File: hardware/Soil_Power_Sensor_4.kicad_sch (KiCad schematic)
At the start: 15 parts, among them J3 UART, J5 Micro_SD_Card, SW1 BOOT, SW2 EN, U8 ESP32-C3-WROOM-02-N4

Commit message: Updated LCSC parts numbers
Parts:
- RN1: MPN (none) -> YC164-JR-1310KL
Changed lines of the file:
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@@
+			)
+		)
+		(property "MPN" " YC164-JR-1310KL"
+			(at 85.09 151.13 0)
+			(effects
+				(font
+					(size 1.27 1.27)
+				)
+				(hide yes)
 			)
 		)
@@
 			)
 		)
+		(property "MPN" " YC164-JR-1310KL"
+			(at 54.61 151.13 0)
+			(effects
+				(font
+					(size 1.27 1.27)
+				)
+				(hide yes)
+			)
+		)
 		(pin "2"
 		)
@@
 			)
 		)
+		(property "MPN" " YC164-JR-1310KL"
+			(at 74.93 151.13 0)
+			(effects
+				(font
+					(size 1.27 1.27)
+				)
+				(hide yes)
+			)
+		)
 		(pin "2"
 		)
@@
 			(at 64.77 151.13 0)
 			(effects
+				(font
+					(size 1.27 1.27)
+				)
+				(hide yes)
+			)
+		)
+		(property "MPN" " YC164-JR-1310KL"
+			(at 64.77 151.13 0)
+			(effects

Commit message: Updated BOM
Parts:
- SW1, SW2: LCSC C93157 -> C2837532
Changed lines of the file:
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@@
 			)
 		)
-		(property "LCSC" "C93157"
+		(property "LCSC" "C2837532"
 			(at 245.11 77.47 0)
 			(effects
@@
 			)
 		)
-		(property "LCSC" "C93157"
+		(property "LCSC" "C2837532"
 			(at 245.11 46.99 0)
 			(effects

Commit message: Regenerated files with kicad-cli script
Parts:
- RN1: LCSC (none) -> C110924
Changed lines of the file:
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@@
+			)
+		)
+		(property "LCSC" "C110924"
+			(at 85.09 151.13 0)
+			(effects
+				(font
+					(size 1.27 1.27)
+				)
+				(hide yes)
 			)
 		)
@@
 			)
 		)
+		(property "LCSC" "C110924"
+			(at 54.61 151.13 0)
+			(effects
+				(font
+					(size 1.27 1.27)
+				)
+				(hide yes)
+			)
+		)
 		(pin "2"
 		)
@@
 			)
 		)
+		(property "LCSC" "C110924"
+			(at 74.93 151.13 0)
+			(effects
+				(font
+					(size 1.27 1.27)
+				)
+				(hide yes)
+			)
+		)
 		(pin "2"
 		)
@@
 			(at 64.77 151.13 0)
 			(effects
+				(font
+					(size 1.27 1.27)
+				)
+				(hide yes)
+			)
+		)
+		(property "LCSC" "C110924"
+			(at 64.77 151.13 0)
+			(effects

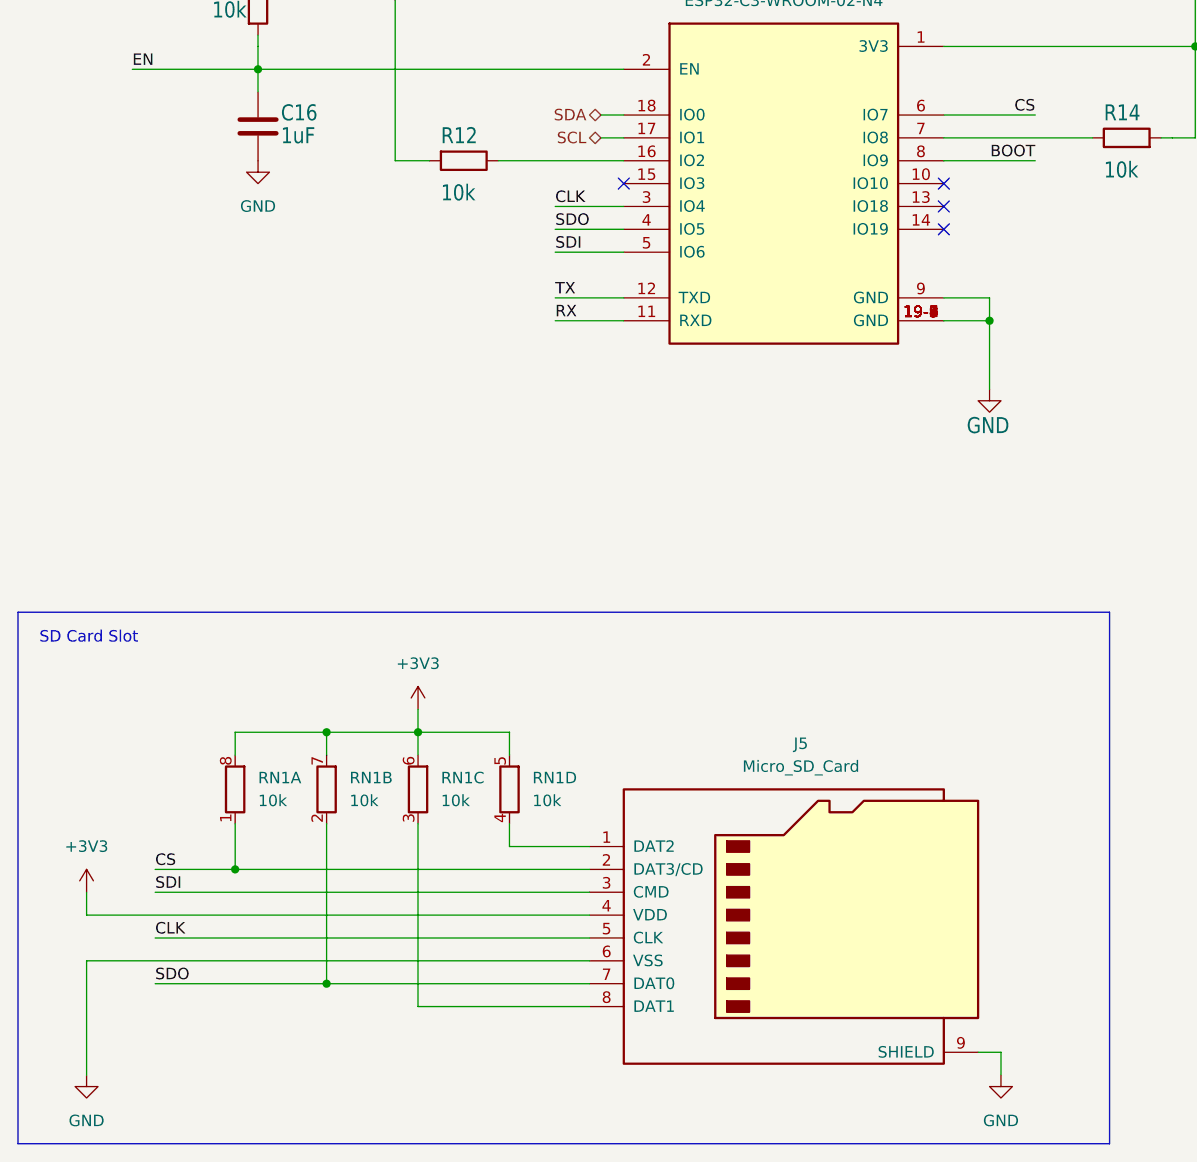
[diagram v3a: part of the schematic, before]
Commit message: Fixed microSD card
Closes #54
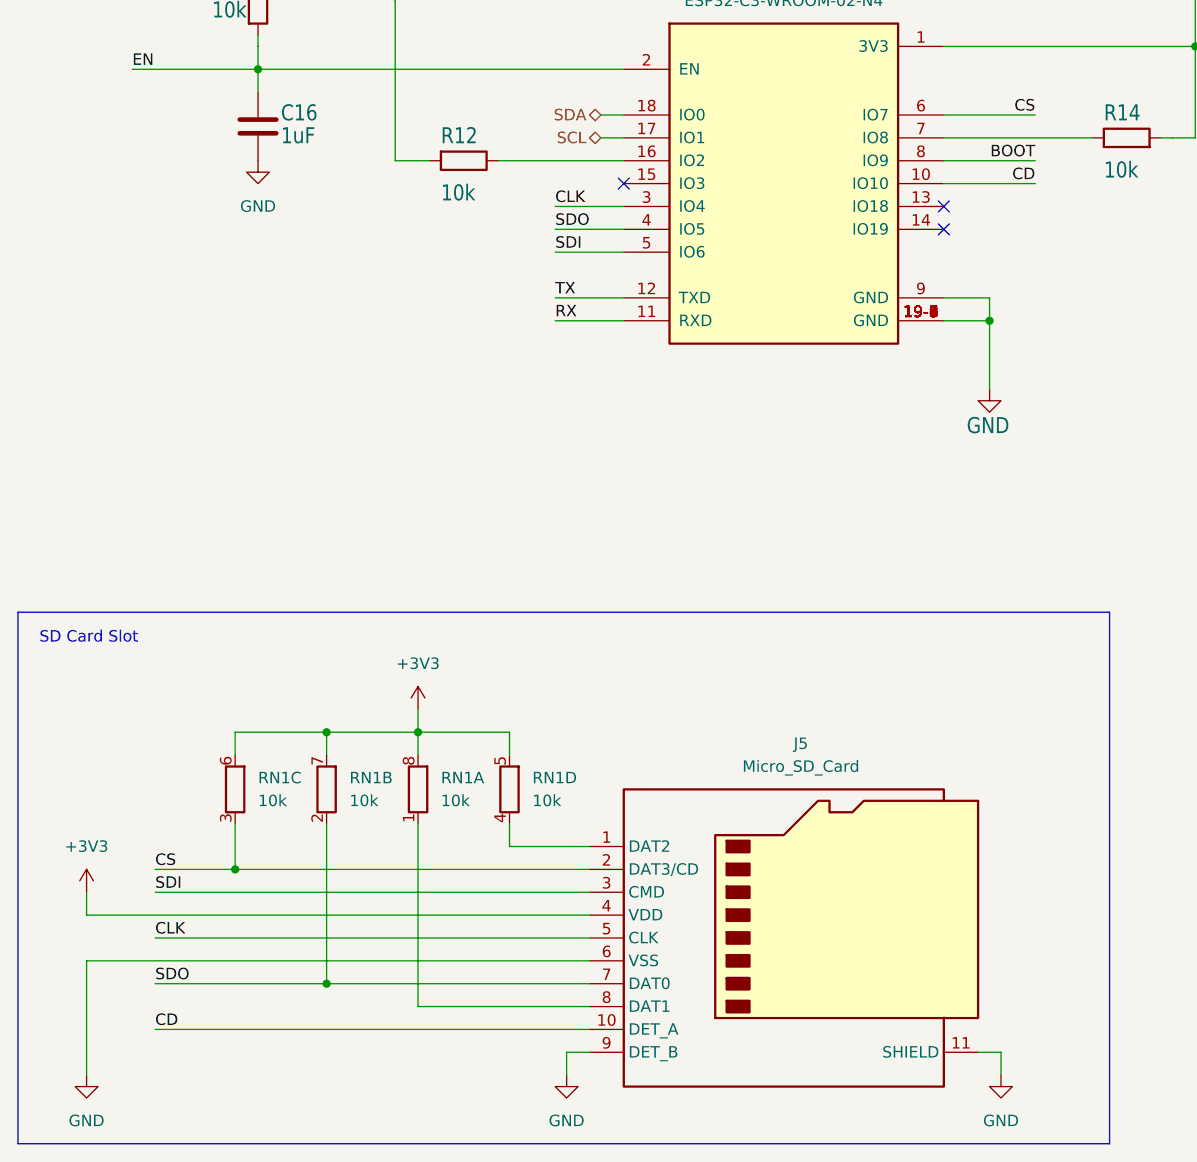
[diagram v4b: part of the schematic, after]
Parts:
- J5: footprint Connector_Card:microSD_HC_Molex_47219-2001 -> Connector_Card:microSD_HC_Molex_104031-0811; symbol Connector:Micro_SD_Card -> Connector:Micro_SD_Card_Det2
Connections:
- net CS: now also RN1.3 (R3.1); no longer RN1.1 (R1.1)
- net GND: now also J5.11 (SHIELD)
- net at J5.8 (DAT1): now also RN1.1 (R1.1); no longer RN1.3 (R3.1)
- net CD: now reaches U8.10 (IO10)
- net CD: now also J5.10 (DET_A)
- no-connect marks 4 -> 3
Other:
- moved on the sheet: RN1A, RN1C
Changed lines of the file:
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@@
-	)
-	(no_connect
-		(at 133.35 83.82)
 	)
 	(no_connect
@@
 	(wire
 		(pts
+			(xy 45.72 177.8) (xy 93.98 177.8)
+		)
+		(stroke
+			(width 0)
+			(type default)
+		)
+	)
+	(wire
+		(pts
 			(xy 54.61 144.78) (xy 64.77 144.78)
+		)
+		(stroke
+			(width 0)
+			(type default)
+		)
+	)
+	(wire
+		(pts
+			(xy 93.98 180.34) (xy 91.44 180.34)
 		)
 		(stroke
@@
 	(wire
 		(pts
+			(xy 91.44 180.34) (xy 91.44 182.88)
+		)
+		(stroke
+			(width 0)
+			(type default)
+		)
+	)
+	(wire
+		(pts
 			(xy 45.72 162.56) (xy 93.98 162.56)
 		)
@@
 		(pts
 			(xy 133.35 76.2) (xy 143.51 76.2)
+		)
+		(stroke
+			(width 0)
+			(type default)
+		)
+	)
+	(wire
+		(pts
+			(xy 133.35 83.82) (xy 143.51 83.82)
 		)
 		(stroke
@@
 		)
 	)
-	(label "SDO"
-		(at 45.72 172.72 0)
+	(label "CD"
+		(at 45.72 177.8 0)
 		(fields_autoplaced yes)
 		(effects
@@
 			)
 			(justify left bottom)
+		)
+	)
+	(label "SDO"
+		(at 45.72 172.72 0)
+		(fields_autoplaced yes)
+		(effects
+			(font
+				(size 1.27 1.27)
+			)
+			(justify left bottom)
+		)
+	)
+	(label "CD"
+		(at 143.51 83.82 180)
+		(fields_autoplaced yes)
+		(effects
+			(font
+				(size 1.27 1.27)
+			)
+			(justify right bottom)
 		)
 	)
@@
 	(symbol
 		(lib_id "Device:R_Pack04_Split")
-		(at 54.61 151.13 0)
+		(at 74.93 151.13 0)
 		(unit 1)
 		(exclude_from_sim no)
@@
 		(fields_autoplaced yes)
 		(property "Reference" "RN1"
-			(at 57.15 149.8599 0)
+			(at 77.47 149.8599 0)
 			(effects
 				(font
@@
 		)
 		(property "Value" "10k"
-			(at 57.15 152.3999 0)
+			(at 77.47 152.3999 0)
 			(effects
 				(font
@@
 		)
 		(property "Footprint" "Resistor_SMD:R_Array_Convex_4x0603"
-			(at 52.578 151.13 90)
+			(at 72.898 151.13 90)
 			(effects
 				(font
@@
 		)
 		(property "Datasheet" "~"
-			(at 54.61 151.13 0)
+			(at 74.93 151.13 0)
 			(effects
 				(font
@@
 		)
 		(property "Description" "4 resistor network, parallel topology, split"
-			(at 54.61 151.13 0)
+			(at 74.93 151.13 0)
 			(effects
 				(font
@@
 		)
 		(property "MPN" " YC164-JR-1310KL"
-			(at 54.61 151.13 0)
+			(at 74.93 151.13 0)
 			(effects
 				(font
@@
 		)
 		(property "LCSC" "C110924"
-			(at 54.61 151.13 0)
+			(at 74.93 151.13 0)
 			(effects
 				(font
@@
 	)
 	(symbol
-		(lib_id "Connector:Micro_SD_Card")
-		(at 116.84 165.1 0)
+		(lib_id "Connector:Micro_SD_Card_Det2")
+		(at 116.84 167.64 0)
 		(unit 1)
 		(exclude_from_sim no)
@@
 			)
 		)
-		(property "Footprint" "Connector_Card:microSD_HC_Molex_47219-2001"
-			(at 146.05 157.48 0)
-			(effects
-				(font
-					(size 1.27 1.27)
-				)
-				(hide yes)
-			)
-		)
-		(property "Datasheet" "http://katalog.we-online.de/em/datasheet/693072010801.pdf"
-			(at 116.84 165.1 0)
-			(effects
-				(font
-					(size 1.27 1.27)
-				)
-				(hide yes)
-			)
-		)
-		(property "Description" "Micro SD Card Socket"
-			(at 116.84 165.1 0)
+		(property "Footprint" "Connector_Card:microSD_HC_Molex_104031-0811"
+			(at 168.91 149.86 0)
+			(effects
+				(font
+					(size 1.27 1.27)
+				)
+				(hide yes)
+			)
+		)
+		(property "Datasheet" "https://www.hirose.com/en/product/document?clcode=&productname=&series=DM3&documenttype=Catalog&lang=en&documentid=D49662_en"
+			(at 119.38 165.1 0)
+			(effects
+				(font
+					(size 1.27 1.27)
+				)
+				(hide yes)
+			)
+		)
+		(property "Description" "Micro SD Card Socket with two card detection pins"
+			(at 116.84 167.64 0)
 			(effects
 				(font
@@
 		)
 		(property "MPN" "472192001"
-			(at 116.84 165.1 0)
+			(at 116.84 167.64 0)
 			(effects
 				(font
@@
 		)
 		(property "MFC" "Molex"
-			(at 116.84 165.1 0)
+			(at 116.84 167.64 0)
 			(effects
 				(font
@@
 		)
 		(property "LCSC" "C164170"
-			(at 116.84 165.1 0)
+			(at 116.84 167.64 0)
 			(effects
 				(font
@@
 		)
 		(pin "4"
+		)
+		(pin "10"
+		)
+		(pin "11"
 		)
 		(instances
@@
 	(symbol
 		(lib_id "Device:R_Pack04_Split")
-		(at 74.93 151.13 0)
+		(at 54.61 151.13 0)
 		(unit 3)
 		(exclude_from_sim no)
@@
 		(fields_autoplaced yes)
 		(property "Reference" "RN1"
-			(at 77.47 149.8599 0)
+			(at 57.15 149.8599 0)
 			(effects
 				(font
@@
 		)
 		(property "Value" "10k"
-			(at 77.47 152.3999 0)
+			(at 57.15 152.3999 0)
 			(effects
 				(font
@@
 		)
 		(property "Footprint" "Resistor_SMD:R_Array_Convex_4x0603"
-			(at 72.898 151.13 90)
+			(at 52.578 151.13 90)
 			(effects
 				(font
@@
 		)
 		(property "Datasheet" "~"
-			(at 74.93 151.13 0)
+			(at 54.61 151.13 0)
 			(effects
 				(font
@@
 		)
 		(property "Description" "4 resistor network, parallel topology, split"
-			(at 74.93 151.13 0)
+			(at 54.61 151.13 0)
 			(effects
 				(font
@@
 		)
 		(property "MPN" " YC164-JR-1310KL"
-			(at 74.93 151.13 0)
+			(at 54.61 151.13 0)
 			(effects
 				(font
@@
 		)
 		(property "LCSC" "C110924"
-			(at 74.93 151.13 0)
+			(at 54.61 151.13 0)
 			(effects
 				(font
@@
 				)
 			)
+		)
+	)
+	(symbol
+		(lib_id "power:GND")
+		(at 91.44 182.88 0)
+		(unit 1)
+		(exclude_from_sim no)
+		(in_bom yes)
+		(on_board yes)
+		(dnp no)
+		(property "Reference" "#PWR035"
+			(at 91.44 189.23 0)
+			(effects
+				(font
+					(size 1.27 1.27)
+				)
+				(hide yes)
+			)
+		)
+		(property "Value" "GND"
+			(at 91.44 187.96 0)
+			(effects
+				(font
+					(size 1.27 1.27)
+				)
+			)
+		)
+		(property "Footprint" ""
+			(at 91.44 182.88 0)
+			(effects
+				(font
+					(size 1.27 1.27)
+				)
+				(hide yes)
+			)
+		)
+		(property "Datasheet" ""
+			(at 91.44 182.88 0)
+			(effects
+				(font
+					(size 1.27 1.27)
+				)
+				(hide yes)
+			)
+		)
+		(property "Description" "Power symbol creates a global label with name \"GND\" , ground"
+			(at 91.44 182.88 0)
+			(effects
+				(font
+					(size 1.27 1.27)
+				)
+				(hide yes)
+			)
+		)
+		(pin "1"
+		)
+		(instances
+			(project ""
+				(path "/5300ec4d-4648-40a1-8d89-4fa6b3bf32a3/1383843a-880b-4efd-8c7f-ecdf3639f794"
+					(reference "#PWR035")
+					(unit 1)
+				)
+			)

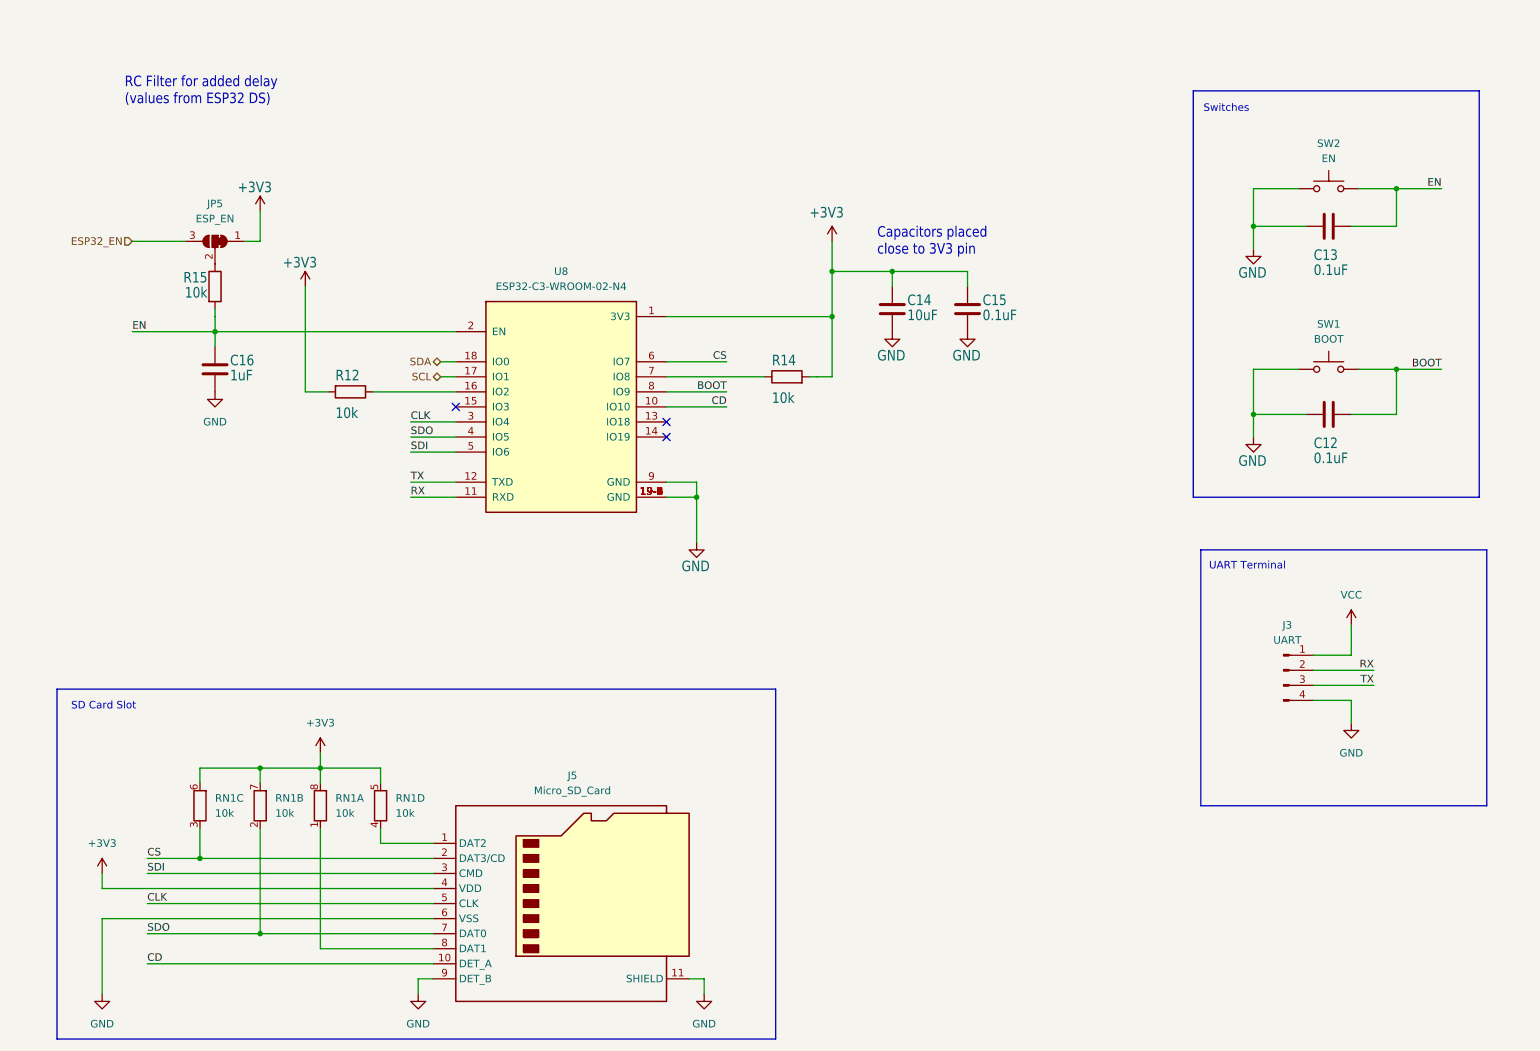
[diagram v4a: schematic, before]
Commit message: Added wakeup line for esp32
Closes #48
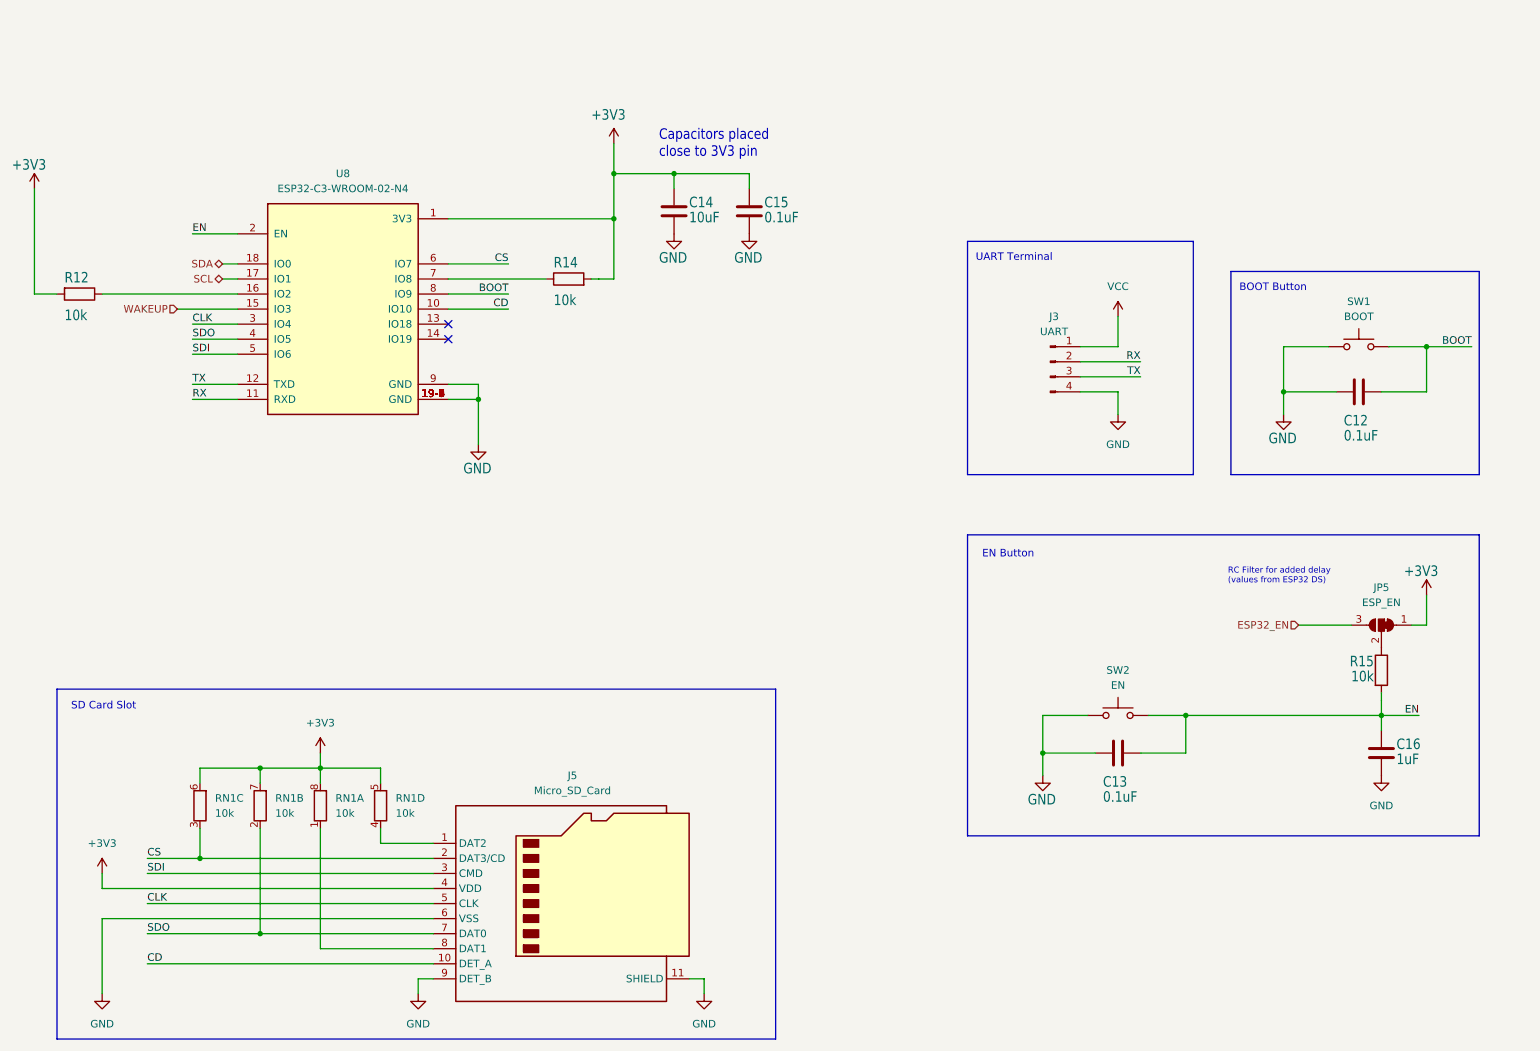
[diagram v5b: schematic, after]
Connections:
- net WAKEUP: now reaches U8.15 (IO3)
- no-connect marks 3 -> 2
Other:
- note added: "BOOT Button"
- note added: "EN Button"
- note removed: "Switches"
- moved on the sheet: C12, C13, C14, C15, C16, J3, JP5, R12, R14, R15, SW1, SW2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

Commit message: Fixed misc issues during ordering
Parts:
- J5: LCSC C164170 -> C585350; MPN 472192001 -> 1040310811
- SW1, SW2: LCSC C2837532 -> C221766; MPN B3F-1000 -> KSC741JLFS
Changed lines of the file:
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@@
 			)
 		)
-		(property "MPN" "B3F-1000"
+		(property "MPN" "KSC741JLFS"
 			(at 250.19 73.66 0)
 			(effects
@@
 			)
 		)
-		(property "LCSC" "C2837532"
+		(property "LCSC" "C221766"
 			(at 250.19 73.66 0)
 			(effects
@@
 			)
 		)
-		(property "MPN" "472192001"
+		(property "MPN" "1040310811"
 			(at 116.84 167.64 0)
 			(effects
@@
 			)
 		)
-		(property "LCSC" "C164170"
+		(property "LCSC" "C585350"
 			(at 116.84 167.64 0)
 			(effects
@@
 			)
 		)
-		(property "MPN" "B3F-1000"
+		(property "MPN" "KSC741JLFS"
 			(at 209.55 135.89 0)
 			(effects
@@
 			)
 		)
-		(property "LCSC" "C2837532"
+		(property "LCSC" "C221766"
 			(at 209.55 135.89 0)
 			(effects
